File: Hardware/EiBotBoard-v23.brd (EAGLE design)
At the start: 56.9 x 56.9 mm, 105 parts, among them IC1 A4983ALT1, IC2 A4983ALT1, IC3 PIC18F46J50-I/PT, IC4 LM317MABDT, IC5 LM317MABDT, J3 USBSMD, J4 IO, J5 IO, J6 POWER_JACKSMD, J7 POWER_JACKSMD, J8 ICSP, SW1 PRG, SW2 RST

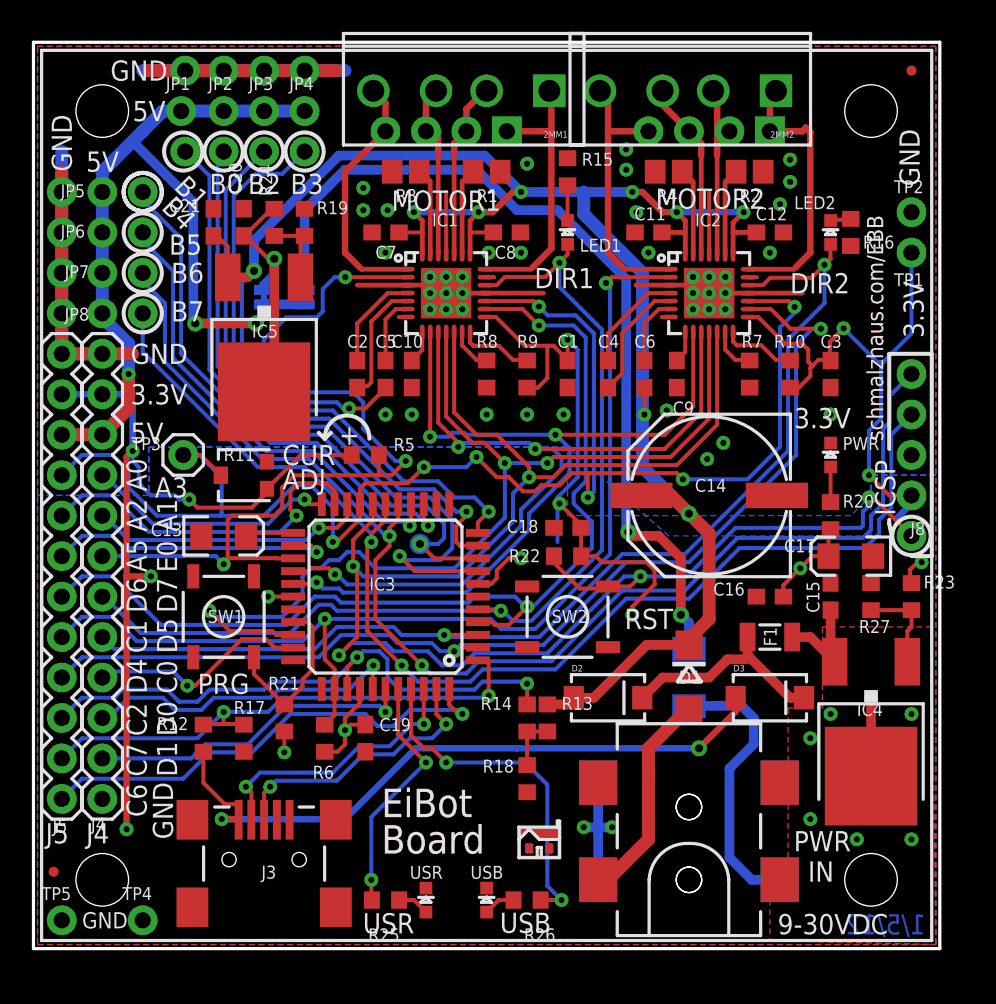
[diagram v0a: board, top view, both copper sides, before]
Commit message: Version 2.3 from Schmalz Haus. This is the latest version that is in production at SeeedStudios (EMSL) and is shipping with EggBot and WatercolorBot. See changes.txt and schematic for list of changes from v2.1 (the latest version SparkFun is producing as of 3/30/2015) to version 2.3. Also adding BOM in.
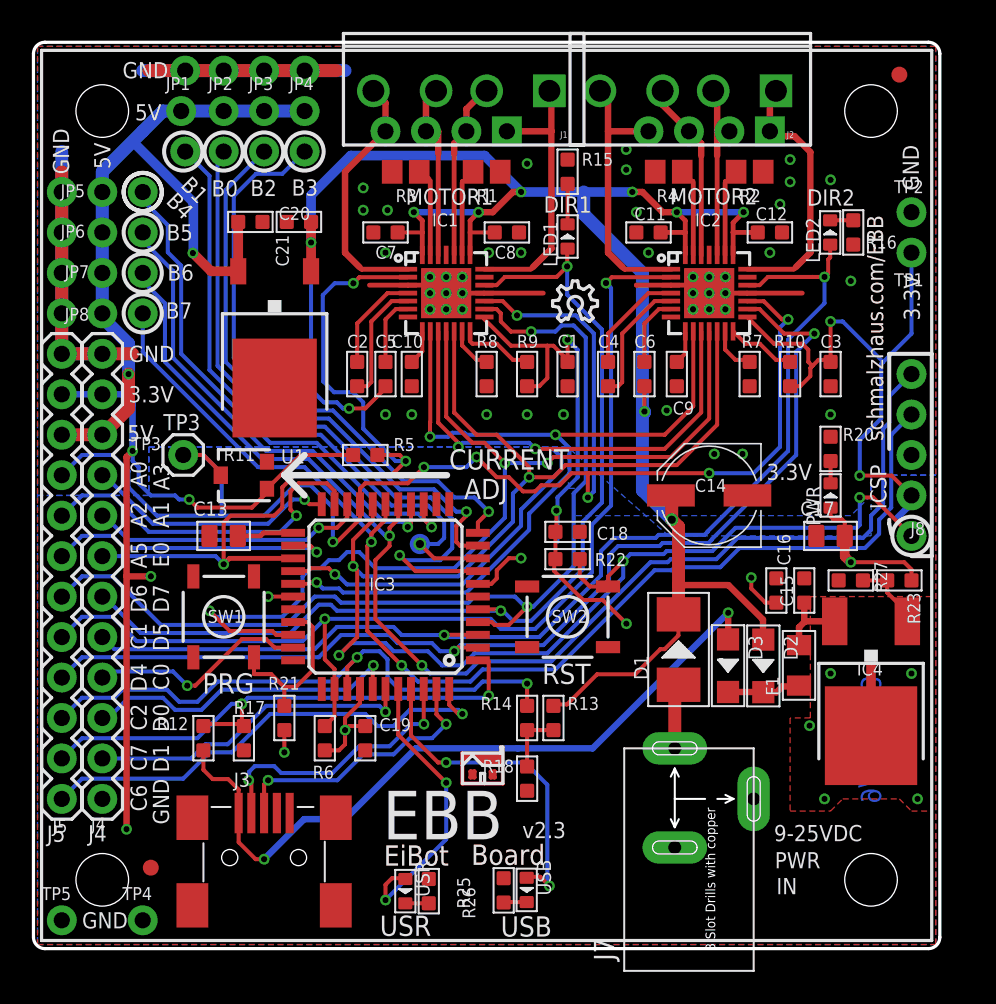
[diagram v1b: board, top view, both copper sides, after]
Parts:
- removed D4: (no value), diode:SOD-123_MINI-SMA
- removed IC5: LM317MABDT, v-reg:DPACK
- removed J6: POWER_JACKSMD, SparkFun11_03_09:POWER_JACK_SMD
- removed JP11: LOGO-SFENEW, SparkFun-12-01-09:SFE-NEW-WEBLOGO
- removed JP12, JP13: (no value), SparkFun-12-01-09:SJ_2S-NO
- removed R19: 715, rcl:R0603
- removed R24: 240, rcl:R0603
- removed U$10, U$11, U$6, U$7, U$8, U$9: PAD, Testing:PAD-0.008
- added LOGO1: OSHW_LOGO_8MILX0100-NT, OSHW:OSHW_8X100_NOTEXT
- added U1: CJ78M05-1300040P1, OPL Eagle Library:TO252
- C1, C10, C11, C12, C15, C16, C18, C19, C2, C3, C4, C5, C6, C7, C8, C9: device SparkFun-2-11-09:0603 -> OPL Eagle Library:C0603
- C13, C17: device SparkFun-2-11-09:EIA3216 -> OPL Eagle Library:C0805
- C14: device SparkFun:PANASONIC_G -> SparkFun:PANASONIC_D
- C20: value 1uF -> .1uF; device SparkFun-2-11-09:0603 -> OPL Eagle Library:C0603
- C21: value .1uf -> 1uF; device SparkFun-2-11-09:0603 -> OPL Eagle Library:C0603
- D1: value (none) -> SS54B; device diode:DO214AC -> OPL Eagle Library:SMB
- D2, D3: value (none) -> SS0520-7-F; device SparkFun:SMA-DIODE -> OPL Eagle Library:SOD123
- F1: value PTCSMD -> FUSE-1206, 500mA; device SchmalzHaus:PTC-1206 -> OPL Eagle Library:F1206
- IC1, IC2: value A4983ALT1 -> A4983; device Testing:QFN-28-5MM_ALT1 -> SchmalzHaus:QFN28
- J3: value USBSMD -> MINI-USB-5P-3400020P1; device SchmalzHaus:USB-MINIB -> OPL Eagle Library:MINI-B-SMD
- J7: value POWER_JACKSMD -> JACK-DC-3P-3410020P1; device SparkFun11_03_09:POWER_JACK_SMD -> OPL Eagle Library:PW-3P-2.1
- JP14, JP15: value FIDUCIALUFIDUCIAL -> FIDUCIAL1X2; device SparkFun:MICRO-FIDUCIAL -> SparkFun:FIDUCIAL-1X2
- LED1: value DIR1_RED -> RED; device SparkFun-2-11-09:LED-0603 -> OPL Eagle Library:LED0603
- LED2: value DIR2_RED -> RED; device SparkFun-2-11-09:LED-0603 -> OPL Eagle Library:LED0603
- PWR, USB, USR: device SparkFun-2-11-09:LED-0603 -> OPL Eagle Library:LED0603
- R10, R15, R16, R20, R21, R22, R23, R25, R26, R27, R5, R6, R7, R8, R9: device rcl:R0603 -> OPL Eagle Library:R0603
- R12, R14: value 47K -> 4.7K; device rcl:R0603 -> OPL Eagle Library:R0603
- R13: value 47K -> 8.2K; device rcl:R0603 -> OPL Eagle Library:R0603
- R17: value 68.1K -> 8.2K; device rcl:R0603 -> OPL Eagle Library:R0603
- R18: value 4.7K -> 1K; device rcl:R0603 -> OPL Eagle Library:R0603
- moved JP14 73.0 mm to (53.8, 54.4)
- moved JP15 69.2 mm to (6.86, 4.57)
- moved D2 9.95 mm to (45.3, 17.2), turned to 270 degrees
- moved U$1 5.85 mm to (27.7, 9.86)
- moved C21 5.36 mm to (16.2, 45.1), turned to 0 degrees
- moved R20 4.19 mm to (49.5, 30.9)
- moved D3 3.31 mm to (43.1, 17.3), turned to 270 degrees
- moved R25 2.77 mm to (24.3, 3.10), turned to 270 degrees
- moved USB 2.59 mm to (30.5, 3.17), turned to 270 degrees
- moved F1 2.55 mm to (47.5, 17.3), turned to 90 degrees
- moved IC4 2.54 mm to (52.1, 15.2)
- moved PWR 2.54 mm to (49.5, 27.9), turned to 90 degrees
- moved D1 1.88 mm to (40.0, 18.3), turned to 90 degrees
- moved C17 1.80 mm to (49.5, 25.4), turned to 0 degrees
- moved C15 1.69 mm to (47.9, 22.0)
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- renumbered 2MM1 to J1, 2MM2 to J2
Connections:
- removed net 5V_ALT: C20.2, IC5.4, JP13.1, R24.2
- removed net N$12: IC1.P$20, U$11.P$1
- removed net N$13: IC1.P$25, U$10.P$1
- removed net N$14: IC2.P$7, U$6.P$1
- removed net N$15: IC2.P$20, U$7.P$1
- removed net N$18: IC2.P$25, U$8.P$1
- removed net N$26: LED2.C, R16.2
- removed net N$27: PWR.A, R20.1
- removed net N$29: R26.1, USB.A
- removed net N$30: R25.1, USR.A
- removed net N$35: LED1.C, R15.2
- new net N$1: LED2.-, R16.2
- net 3.3V: now also C17.2, PWR.+; no longer C17.A, R20.2
- net 5V_SVO: now also C20.2, U1.3; no longer JP12.2, JP13.2
- net D+: now also J3.3; no longer J3.D+
- net D-: now also J3.2; no longer J3.D-
- net DIR_1: now also LED1.+; no longer LED1.A
- net DIR_2: now also LED2.+; no longer LED2.A
- net GND: now also C13.1, C17.1, J3.5, J3.P$1, J3.P$2, J3.P$3, J3.P$4, J7.-1, R20.1, R25.1, R26.1, U1.2; no longer C13.C, C17.C, J3.GND, J3.GND@3, J3.GND@4, J6.GND, J6.P$4, J7.GND, J7.P$4, PWR.C, R19.2, USB.C, USR.C
- net N$10: now also R25.2, USR.-; no longer D4.C, JP12.1
- net N$11: now also PWR.-, R20.2; no longer IC1.P$7, U$9.P$1
- net N$2: now also D2.-, D3.-; no longer D2.C, D3.C
- net N$6: now also D1.+, J7.+; no longer D1.A, J7.VIN0
- net N$7: now also LED1.-, R15.2; no longer D4.A, J6.VIN0
- net N$8: now also R26.2, USB.-; no longer IC5.1, R19.1, R24.1
- net USB_LED: now also USB.+; no longer R26.2
- net USR_LED: now also USR.+; no longer R25.2
- net V+: now also D1.-, D2.+, U1.1; no longer D1.C, D2.A, IC5.3
- net VBUS: now also D3.+, J3.1; no longer D3.A, J3.VBUS
- net VCAP: now also C13.2; no longer C13.A
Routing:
- net N$10: track 54.9 -> 1.47 mm, vias 2 -> 0
- net 5V_ALT: track 16.2 -> 0.00 mm, vias 1 -> 0
- net N$7: track 17.5 -> 2.54 mm
- net N$6: track 13.5 -> 4.24 mm
- net N$2: track 13.7 -> 4.63 mm
- net GND: track 84.2 -> 75.6 mm
- net 5V_SVO: track 56.5 -> 50.7 mm, vias 3 -> 2
- net ENABLE_1: track 54.9 -> 50.2 mm
- net V+: track 131.2 -> 126.7 mm
- net N$18: track 3.91 -> 0.00 mm
- net N$13: track 3.91 -> 0.00 mm
- net VBUS: track 42.7 -> 46.6 mm
- net 3.3V: track 150.6 -> 154.3 mm, vias 22 -> 21
- net N$8: track 5.14 -> 1.46 mm
- net USR_LED: track 15.4 -> 18.6 mm
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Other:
- outline, holes or cut-outs redrawn
- board text added: "9-25VDC"
- board text added: "9/11/2013"
- board text added: "CURRENT"
- board text added: "EBB"
- board text added: "TP3"
- board text added: "v2.3"
- board text removed: "+"
- board text removed: "1/5/12"
- board text removed: "4-6V DC"
- board text removed: "9-30VDC"
- board text removed: "CUR"
- board text removed: "JP12"
- board text removed: "JP13"

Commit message: Updating part numbers to SFE libraries, swapping vregs
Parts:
- removed C13, C17: 10uF, OPL Eagle Library:C0805
- removed D2, D3: SS0520-7-F, OPL Eagle Library:SOD123
- removed J1, J2: (no value), EiBotBoard-v21:SCHMALZHAUS_SCREWTERMINAL-3.5MM-4_LOCK
- removed J3: MINI-USB-5P-3400020P1, OPL Eagle Library:MINI-B-SMD
- removed J7: JACK-DC-3P-3410020P1, OPL Eagle Library:PW-3P-2.1
- removed LED1, LED2, USR: RED, OPL Eagle Library:LED0603
- removed PWR, USB: GREEN, OPL Eagle Library:LED0603
- removed SW1: PRG, SparkFunEagle-6-6-07:TACTILE_SWITCH_SMD
- removed SW2: RST, SparkFunEagle-6-6-07:TACTILE_SWITCH_SMD
- removed U1: CJ78M05-1300040P1, OPL Eagle Library:TO252
- added C22, C23: 10uF, SparkFun-Capacitors:EIA3216
- added D10: PMEG4005EJ, SparkFun-DiscreteSemi:SOD-323
- added D4, D5, D6: RED, SparkFun-LED:LED-0603
- added D7, D8: GREEN, SparkFun-LED:LED-0603
- added D9: B340A, SparkFun-DiscreteSemi:SMA-DIODE
- added IC5: V_REG_317DPACK, SparkFun-PowerIC:V-REG_DPACK
- added JP11: POWER_JACKPTH_LOCK, SparkFun-Connectors:POWER_JACK_PTH_LOCK
- added JP12: USBSMD, SparkFun-Connectors:USB-MINIB
- added JP13, JP16, JP17, JP18: (no value), SparkFun-Connectors:SCREWTERMINAL-3.5MM-2_LOCK
- added LOGO2: SFE_LOGO_FLAME.2_INCH, SparkFun-Aesthetics:SFE_LOGO_FLAME_.2
- added LOGO3: SFE_LOGO_NAME_FLAME.2_INCH, SparkFun-Aesthetics:SFE_LOGO_NAME_FLAME_.2
- added R19: 240, SparkFun-Resistors:0603-RES
- added R24: 715, SparkFun-Resistors:0603-RES
- added S1, S2: SWITCH-MOMENTARY-2SMD, SparkFun-Electromechanical:TACTILE-SWITCH-SMD
- C1, C11, C12, C15, C18, C19, C2, C3, C4, C5, C6, C7, C8: value .1uf -> 0.1uF; device OPL Eagle Library:C0603 -> SparkFun-Capacitors:0603-CAP
- C10, C9: value .22uF -> 0.22uF; device OPL Eagle Library:C0603 -> SparkFun-Capacitors:0603-CAP
- C14: device SparkFun:PANASONIC_D -> SparkFun-Capacitors:NIC_10X10.5_CAP
- C16, C21: value 1uF -> 1.0uF; device OPL Eagle Library:C0603 -> SparkFun-Capacitors:0603-CAP
- C20: value .1uF -> 0.1uF; device OPL Eagle Library:C0603 -> SparkFun-Capacitors:0603-CAP
- D1: value SS54B -> PMEG4005EJ; device OPL Eagle Library:SMB -> SparkFun-DiscreteSemi:SOD-323
- F1: device OPL Eagle Library:F1206 -> SparkFun-PowerIC:PTC-1206
- IC1, IC2: value A4983 -> A49831:1; device SchmalzHaus:QFN28 -> SparkFun-PowerIC:QFN-28-5MM-1:1
- IC3: device SchmalzHaus:TQFP44 -> Testing:TQFP44
- IC4: value LM317MABDT -> V_REG_317DPACK; device v-reg:DPACK -> SparkFun-PowerIC:V-REG_DPACK
- J4, J5: device SparkFun-12-01-09:1X12 -> SparkFun-Connectors:1X12
- J8: device SchmalzHaus:1X05_NOSILK -> SparkFun-Connectors:1X05_NO_SILK
- JP1: device SparkFun:1X03_LOCK_NO_SILK -> SparkFun-Connectors:1X03_LOCK_NO_SILK
- JP10, JP9: device SparkFun-12-01-09:MOLEX-1X4 -> SparkFun-Connectors:MOLEX-1X4
- JP14, JP15: device SparkFun:FIDUCIAL-1X2 -> SparkFun-Aesthetics:FIDUCIAL-1X2
- JP2, JP3, JP4, JP5, JP6, JP7, JP8: device SparkFun-12-01-09:1X03_NO_SILK -> SparkFun-Connectors:1X03_LOCK_NO_SILK
- LOGO1: value OSHW_LOGO_8MILX0100-NT -> OSHW-LOGOS; device OSHW:OSHW_8X100_NOTEXT -> SparkFun-Aesthetics:OSHW-LOGO-S
- R1, R2, R3, R4: value .22 -> 0.22; device rcl:R0805 -> SparkFun-Resistors:0805
- R10, R12, R13, R14, R15, R16, R17, R18, R20, R21, R22, R23, R25, R26, R27, R5, R6, R7, R8, R9: device OPL Eagle Library:R0603 -> SparkFun-Resistors:0603-RES
- R11: value TRIMPOTSMD - 10K -> 10k; device SparkFun11_03_09:TRIMPOT-3MM -> SparkFun-Electromechanical:TRIMPOT-3MM
- TP3: device SchmalzHaus:1X01 -> SparkFun-Connectors:1X01
- TP6: device SparkFun:PAD.03X.05 -> SparkFun-Passives:PAD.03X.05
- U$2, U$3, U$4, U$5: device SparkFun01082009:STAND-OFF -> SparkFun-Electromechanical:STAND-OFF
- moved C20 8.66 mm to (9.50, 37.2), turned to 270 degrees
- moved C21 3.81 mm to (12.3, 45.1)
- moved D1 3.43 mm to (43.2, 17.0)
- moved LOGO1 1.80 mm to (33.4, 40.1)
- moved R23 0.45 mm to (54.2, 22.3)
- moved R27 0.32 mm to (50.8, 22.3)
- moved U$1 0.32 mm to (27.7, 10.2)
- moved R20 0.32 mm to (49.5, 31.2)
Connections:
- new net N$12: IC5.1, R19.1, R24.2
- net 3.3V: now also C23.A, D7.A; no longer C17.2, PWR.+
- net 5V_SVO: now also IC5.4, R19.2; no longer U1.3
- net D+: now also JP12.D+; no longer J3.3
- net D-: now also JP12.D-; no longer J3.2
- net DIR_1: now also D5.A; no longer LED1.+
- net DIR_2: now also D6.A; no longer LED2.+
- net GND: now also C22.C, C23.C, JP11.GND, JP11.GNDBREAK, JP12.GND, R24.1, S1.1, S2.1; no longer C13.1, C17.1, J3.5, J3.P$1, J3.P$2, J3.P$3, J3.P$4, J7.-1, SW1.4, SW2.1, U1.2
- net M1_OUT1A: now also JP13.2; no longer J1.2
- net M1_OUT1B: now also JP13.1; no longer J1.1
- net M1_OUT2A: now also JP16.1; no longer J1.3
- net M1_OUT2B: now also JP16.2; no longer J1.4
- net M2_OUT1A: now also JP17.2; no longer J2.2
- net M2_OUT1B: now also JP17.1; no longer J2.1
- net M2_OUT2A: now also JP18.1; no longer J2.3
- net M2_OUT2B: now also JP18.2; no longer J2.4
- net MCLR: now also S2.3; no longer SW2.3
- net N$1: now also D6.C; no longer LED2.-
- net N$10: now also D4.C; no longer USR.-
- net N$11: now also D7.C; no longer PWR.-
- net N$2: now also D1.C, D10.C; no longer D2.-, D3.-
- net N$6: now also D9.A, JP11.PWR; no longer D1.+, J7.+
- net N$7: now also D5.C; no longer LED1.-
- net N$8: now also D8.C; no longer USB.-
- net PRG_SW: now also S1.3; no longer SW1.2
- net USB_LED: now also D8.A; no longer USB.+
- net USR_LED: now also D4.A; no longer USR.+
- net V+: now also D10.A, D9.C, IC5.3; no longer D1.-, D2.+, U1.1
- net VBUS: now also D1.A, JP12.VBUS; no longer D3.+, J3.1
- net VCAP: now also C22.A; no longer C13.2
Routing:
- net V+: track 126.7 -> 135.9 mm
- net 5V_SVO: track 50.7 -> 55.3 mm, vias 2 -> 1
- net N$12: track 0.00 -> 4.33 mm
- net N$6: track 4.24 -> 6.00 mm
- net VBUS: track 46.6 -> 48.0 mm
- net REF_RA0: track 96.2 -> 97.5 mm
- net USR_LED: track 18.6 -> 17.3 mm
- net M1_OUT2A: track 11.3 -> 10.6 mm
- net STEP_1: track 62.3 -> 61.6 mm
- net M1_OUT2B: track 15.9 -> 16.5 mm
- net VCAP: track 3.55 -> 3.01 mm
- net M1_OUT1A: track 11.4 -> 10.9 mm
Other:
- board text added: "4/1/2015"
- board text added: "v2.4"
- board text removed: "9/11/2013"
- board text removed: "v2.3"

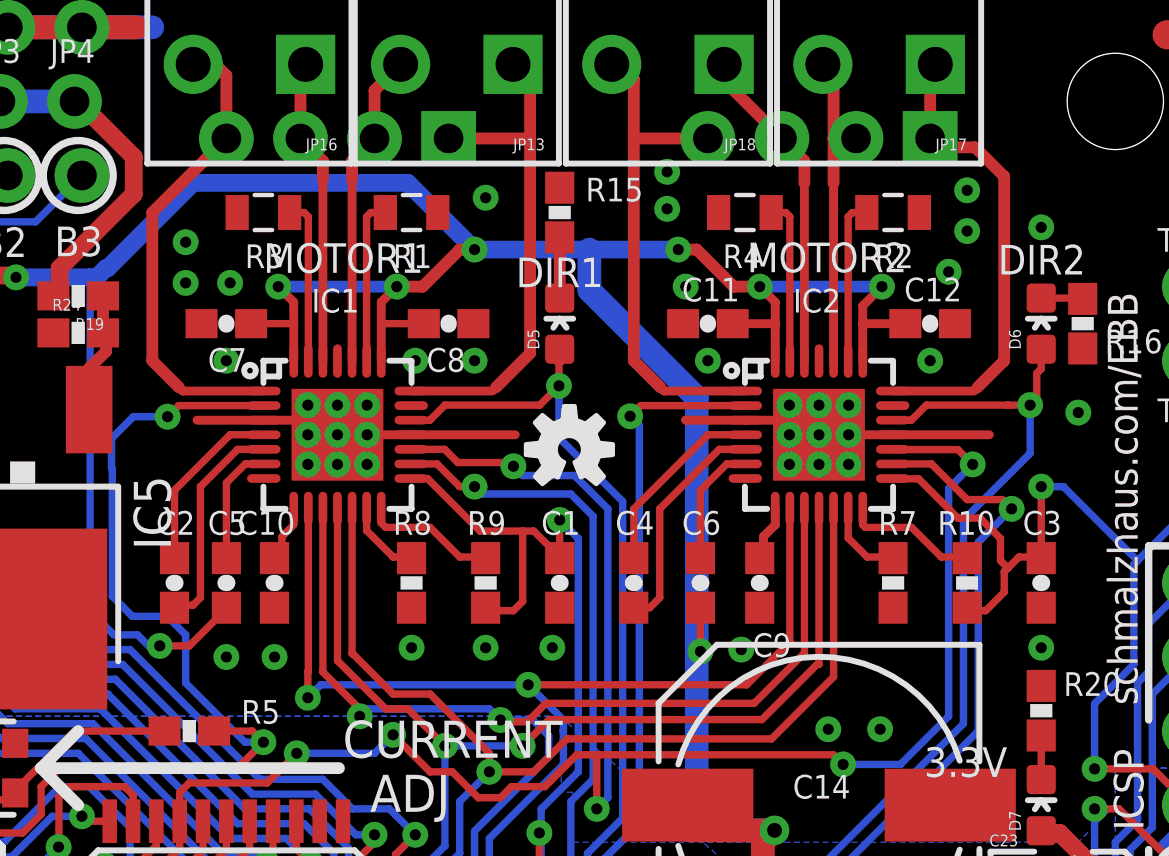
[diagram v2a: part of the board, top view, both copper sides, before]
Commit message: Updating to A4988 ICs
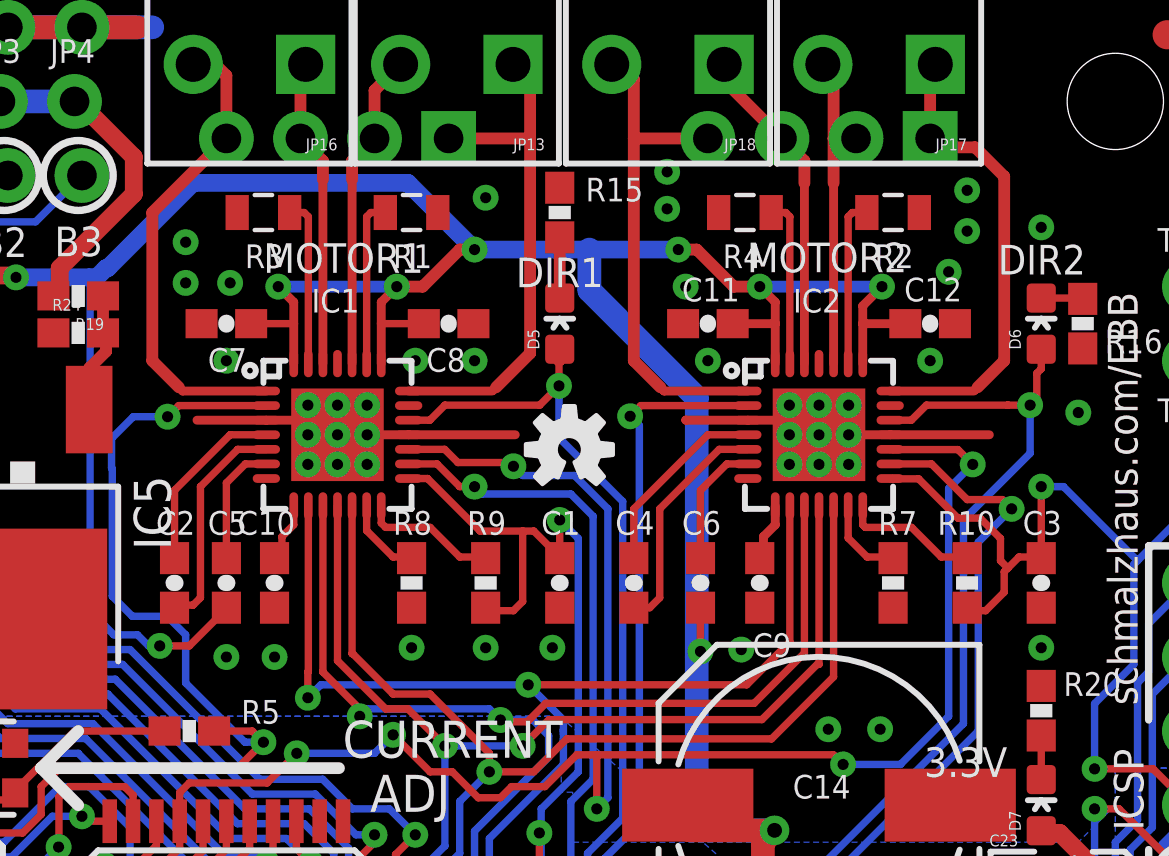
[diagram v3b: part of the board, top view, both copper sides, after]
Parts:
- IC1, IC2: value A49831:1 -> A4988ALT1; device SparkFun-PowerIC:QFN-28-5MM-1:1 -> SparkFun-PowerIC:QFN-28-5MM_ALT1

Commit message: Updating additional packages, fixing DRC errors
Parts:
- D1, D10: value PMEG4005EJ -> MBRA140; device SparkFun-DiscreteSemi:SOD-323 -> SparkFun-DiscreteSemi:SMA-DIODE
- moved D1 2.78 mm to (43.7, 14.3), turned to 0 degrees
- moved D10 2.47 mm to (43.6, 18.7), turned to 270 degrees
- moved F1 1.14 mm to (46.9, 18.2)
- moved D9 0.71 mm to (39.2, 18.7)
- moved R26 0.10 mm to (29.0, 3.05)
- moved R25 0.05 mm to (24.3, 3.05)
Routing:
- net V+: track 136.3 -> 132.4 mm
- net VBUS: track 48.0 -> 44.4 mm
- net N$2: track 4.88 -> 5.83 mm
